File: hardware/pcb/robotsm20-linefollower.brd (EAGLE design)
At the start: 160 x 100 mm, 120 parts, among them IC1 BNO055, IC2 TPS43061RTER, Q1 CSD15571Q2, Q2 CSD15571Q2, Q3 CSD15571Q2, Q4 CSD15571Q2, Q5 BSS138LT3G, Q6 BSS138LT3G, Q7 BSS138LT3G, U1 STM32F405RG

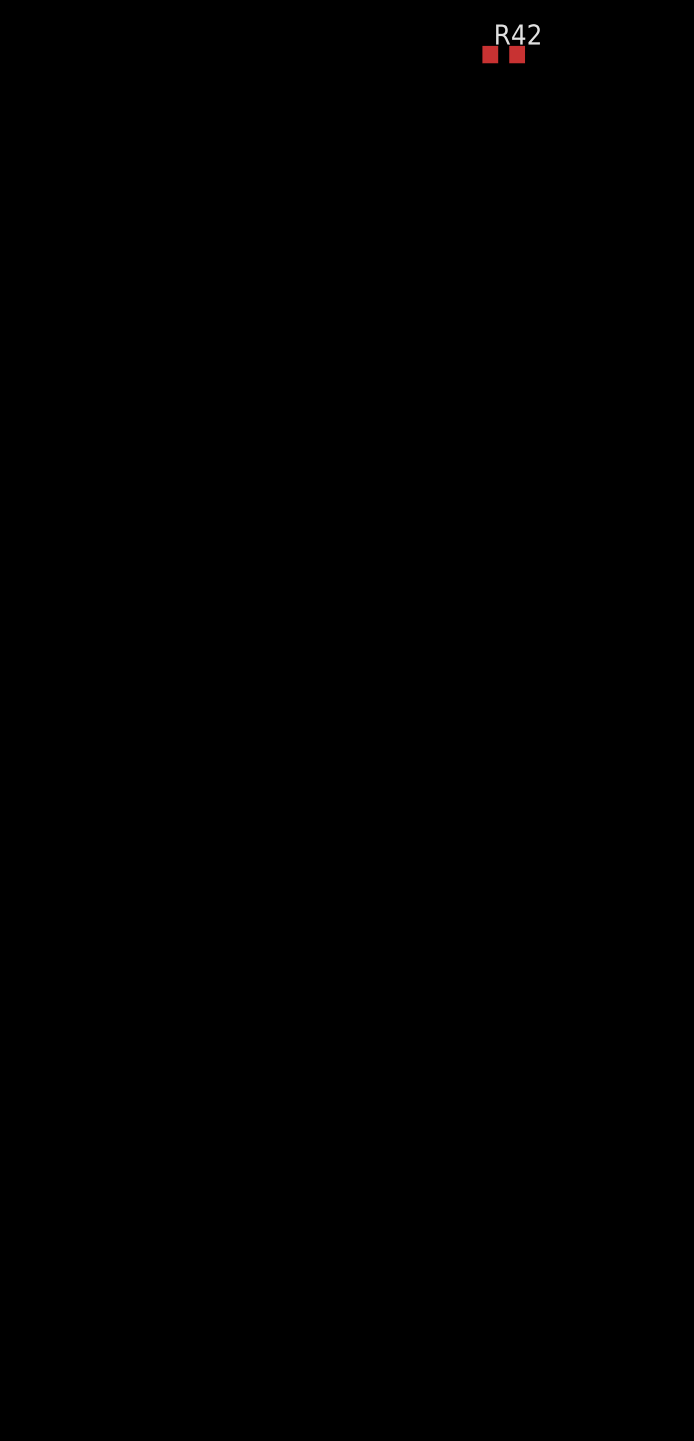
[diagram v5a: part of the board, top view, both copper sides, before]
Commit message: Added more connectors to motors and sensor
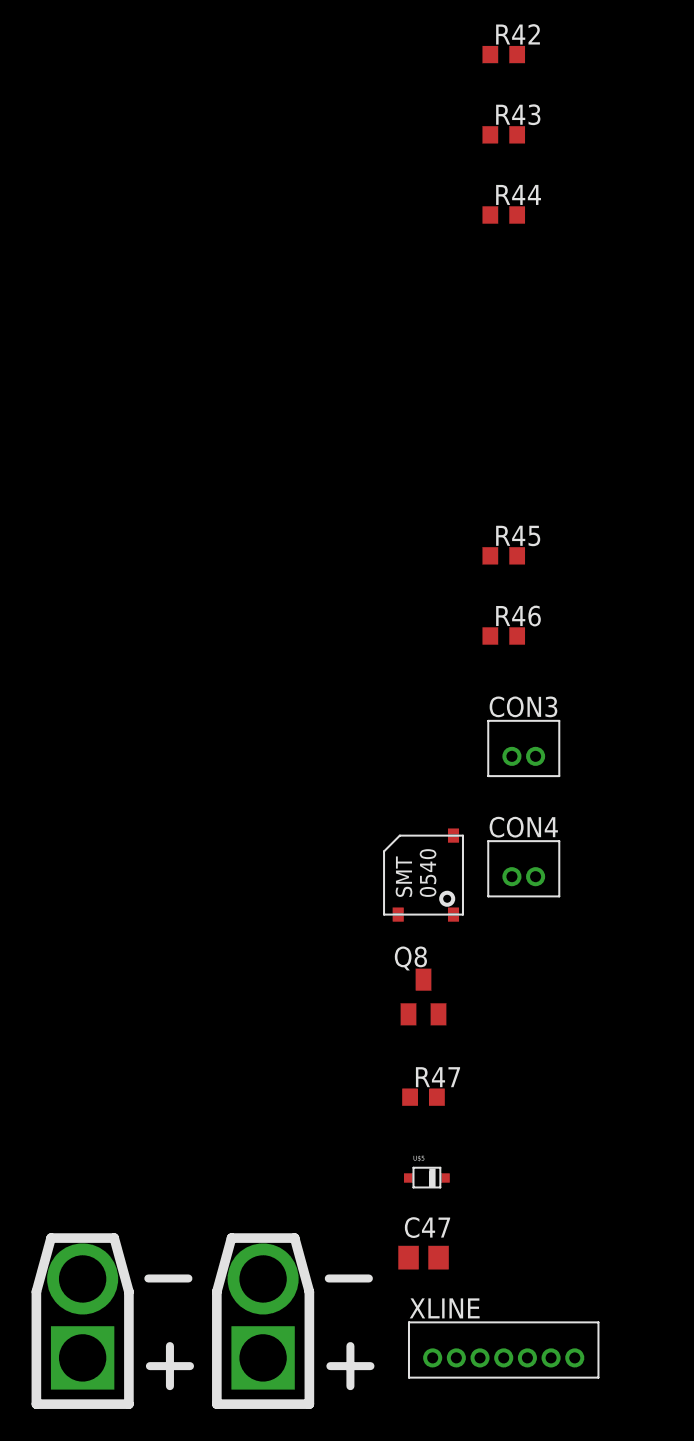
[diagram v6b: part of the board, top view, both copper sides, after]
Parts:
- added C47: (no value), rcl:C0805
- added CON3, CON4: ZR_B2B-ZR, CASE-JST:B2B-ZR
- added Q8: BSS138LT3G, CASE-Transistors:SOT23
- added R43: 20k, rcl:R0603
- added R44, R45, R47: 10k, rcl:R0603
- added R46: 62k, rcl:R0603
- added U$1: SMT-0540-S-R, Isaks Bibliotek:SMT-0540-S-R
- added U$5: DIODE_1N4148WX, Isaks Bibliotek:1N4148WX_SOD-323-2
- added U$8, U$9: XT30, CASE_DC-Connector:XT30
- added XLINE: ZH, CASE-JST:B7B-ZR
- R32: value 245R -> 300R
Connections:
- net N$66 renamed SDIO_CK
- net N$80 renamed SDIO_D0
- net VOLTM_CELL1 renamed N$25
- removed net 3.3V: BOOT.1, BOOT.2, C31.1, C32.1, C33.1, C34.1, C35.1, C37.1, C39.1, R30.1, R31.1, U1.1, U1.13, U1.19, U1.32, U1.48, U1.64
- removed net 3.3V1: R41.1, R42.1
- removed net CURA: C1.1, R3.2
- removed net CURB: C2.1, R4.2
- removed net GND1: PS2.3
- removed net INTERFACE_BUT1: C46.1, R35.1
- removed net N$10: PS2.9, R8.1
- removed net N$25 (its old number): U1.8
- removed net N$35: U1.11
- removed net N$82: U1.37
- removed net N$83: U1.38
- removed net V+1: C14.1, PS2.1, PS2.2
- new net MOTOR_L_CUR: C1.1, R3.2, U1.8
- new net MOTOR_R_CUR: C2.1, R4.2, U1.9
- new net PWM_FAN_L: CON3.1, U1.37
- new net PWM_FAN_R: CON4.1, U1.38
- new net SDIO_CMD: U1.54
- net +12V: now also R46.2
- net +3V3: now also BOOT.1, BOOT.2, C31.1, C32.1, C33.1, C34.1, C35.1, C37.1, C39.1, C47.1, R30.1, R31.1, R41.1, R42.1, U$1.+, U$5.-, U1.1, U1.13, U1.19, U1.32, U1.48, U1.64, XLINE.2
- net BTN_SEL: now also C46.1, R35.1, U1.11; no longer U1.54
- net BUZZER: now also Q8.1, R47.1
- net GND: now also CON3.2, CON4.2, PS2.3, PS2.9, Q8.2, R44.2, R45.1, R47.2, R8.1, U$8.NEG-, U$9.NEG-, XLINE.1
- net MUX0: now also XLINE.4
- net MUX1: now also XLINE.5
- net MUX2: now also XLINE.6
- net MUX3: now also XLINE.7
- net N$33: now also C47.2, Q8.3, U$1.-, U$5.+; no longer U1.9
- net V+: now also C14.1, PS2.1, PS2.2, R43.1, U$8.POS+, U$9.POS+
- net VOLTM_BATT: now also R43.2, R44.1, R45.2, R46.1
- net XLINE: now also XLINE.3

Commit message: Corrected some ERC
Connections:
- removed net N$2: MOTORDRIVER.26, MOTORDRIVER.27
- removed net N$36: C43.1
- net +3V3: now also C43.1
- net 12V: now also MOTORDRIVER.26, MOTORDRIVER.27
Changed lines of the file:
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@@
 <contactref element="XLINE" pad="1"/>
 <contactref element="U$8" pad="NEG-"/>
-<contactref element="U$9" pad="NEG-"/>
 <contactref element="R8" pad="1"/>
 <contactref element="PS2" pad="9"/>
 <contactref element="PS2" pad="3"/>
+<contactref element="U$9" pad="NEG-"/>
 <wire x1="-53.66" y1="-186.69" x2="-53.66" y2="-193.04" width="0" layer="19" extent="1-1"/>
 <wire x1="-53.66" y1="-180.34" x2="-53.66" y2="-186.69" width="0" layer="19" extent="1-1"/>
@@
 <wire x1="124.25" y1="45.3856" x2="123.61" y2="53.34" width="0" layer="19" extent="1-1"/>
 </signal>
-<signal name="N$2">
-<contactref element="MOTORDRIVER" pad="26"/>
-<contactref element="MOTORDRIVER" pad="27"/>
-<wire x1="130.4756" y1="40.16" x2="130.4756" y2="39.66" width="0" layer="19" extent="1-1"/>
-</signal>
 <signal name="12V">
 <contactref element="MOTORDRIVER" pad="10"/>
@@
 <contactref element="C5" pad="1"/>
 <contactref element="C4" pad="1"/>
+<contactref element="MOTORDRIVER" pad="26"/>
+<contactref element="MOTORDRIVER" pad="27"/>
 <wire x1="132.08" y1="37.78" x2="137.16" y2="39.63" width="0" layer="19" extent="1-1"/>
-<wire x1="123.5244" y1="39.66" x2="132.08" y2="37.78" width="0" layer="19" extent="1-1"/>
-<wire x1="123.5244" y1="40.16" x2="123.5244" y2="39.66" width="0" layer="19" extent="1-1"/>
+<wire x1="130.4756" y1="39.66" x2="132.08" y2="37.78" width="0" layer="19" extent="1-1"/>
+<wire x1="130.4756" y1="40.16" x2="130.4756" y2="39.66" width="0" layer="19" extent="1-1"/>
+<wire x1="123.5244" y1="40.16" x2="130.4756" y2="40.16" width="0" layer="19" extent="1-1"/>
+<wire x1="123.5244" y1="39.66" x2="123.5244" y2="40.16" width="0" layer="19" extent="1-1"/>
 <wire x1="121.92" y1="37.78" x2="123.5244" y2="39.66" width="0" layer="19" extent="1-1"/>
 <wire x1="116.84" y1="39.63" x2="121.92" y2="37.78" width="0" layer="19" extent="1-1"/>
@@
 <contactref element="R30" pad="1"/>
 <contactref element="R31" pad="1"/>
+<contactref element="C43" pad="1"/>
 <wire x1="-55.56" y1="-180.34" x2="-55.56" y2="-193.04" width="0" layer="19" extent="1-1"/>
 <wire x1="-55.56" y1="-167.64" x2="-55.56" y2="-180.34" width="0" layer="19" extent="1-1"/>
@@
 <wire x1="-67.83" y1="-80.01" x2="-53.28" y2="-126.4087" width="0" layer="19" extent="1-1"/>
 <wire x1="-67.83" y1="-74.93" x2="-67.83" y2="-80.01" width="0" layer="19" extent="1-1"/>
-<wire x1="-32.17" y1="-27.94" x2="-67.83" y2="-74.93" width="0" layer="19" extent="1-1"/>
+<wire x1="-33.97" y1="-30.48" x2="-67.83" y2="-74.93" width="0" layer="19" extent="1-1"/>
+<wire x1="-32.17" y1="-27.94" x2="-33.97" y2="-30.48" width="0" layer="19" extent="1-1"/>
 <wire x1="-28.92" y1="-26.42" x2="-32.17" y2="-27.94" width="0" layer="19" extent="1-1"/>
 <wire x1="-28.42" y1="-25.12" x2="-28.92" y2="-26.42" width="0" layer="19" extent="1-1"/>
@@
 <wire x1="120.43" y1="4.755" x2="123.61" y2="10.16" width="0" layer="19" extent="1-1"/>
 </signal>
-<signal name="N$1">
-</signal>
 <signal name="N$6">
 <contactref element="R7" pad="1"/>
@@
 <wire x1="-28.92" y1="-26.92" x2="-33.87" y2="-27.94" width="0" layer="19" extent="1-1"/>
 </signal>
-<signal name="N$36">
-<contactref element="C43" pad="1"/>
-</signal>
 <signal name="N$27">

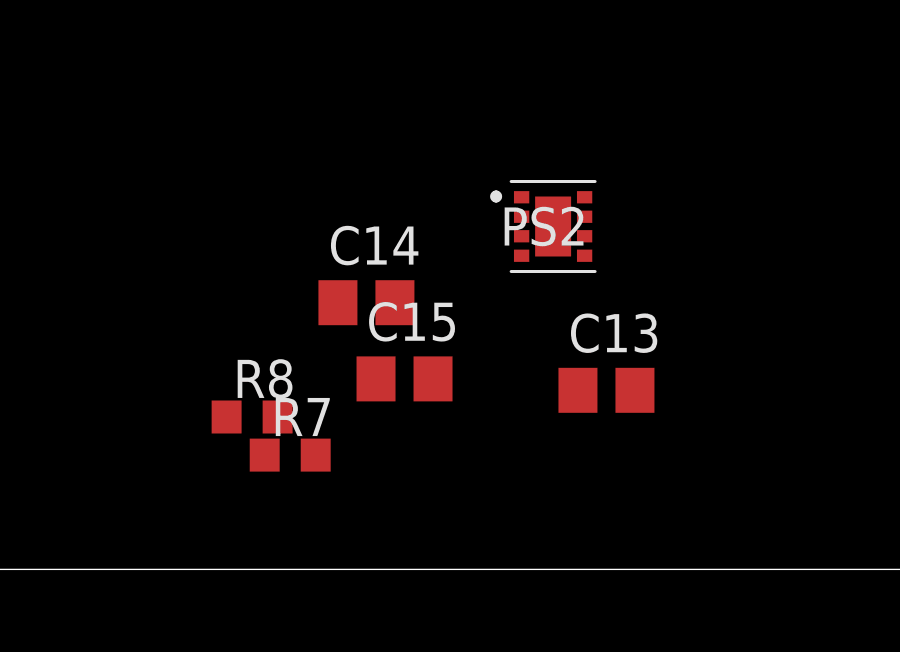
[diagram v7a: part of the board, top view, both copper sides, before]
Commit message: Deleted 3V7 buck
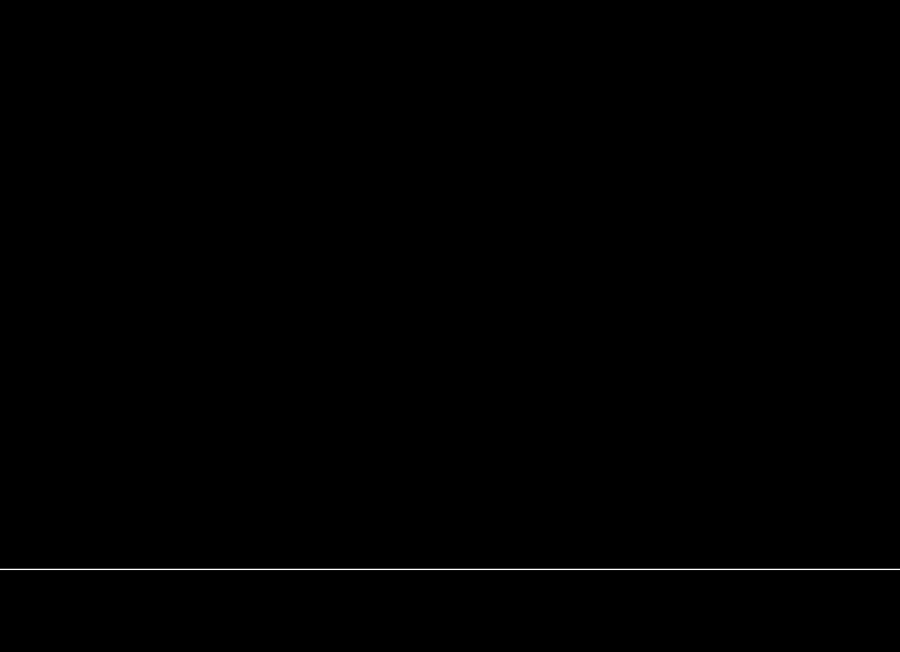
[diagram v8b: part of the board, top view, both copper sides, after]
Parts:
- removed C13, C14: 22µF, rcl:C0805
- removed C15: 3300pF, rcl:C0805
- removed PS2: TPS82130SILT, PowerManagement:TPS82130SILT
- removed R7: 36.25k, rcl:R0603
- removed R8: 10k, rcl:R0603
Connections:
- removed net 3V7: C13.1, PS2.4, PS2.5, R7.2
- removed net N$5: C15.1, PS2.8
- removed net N$6: PS2.6, R7.1, R8.2
- net GND: no longer C13.2, C14.2, C15.2, PS2.3, PS2.9, R8.1
- net V+: no longer C14.1, PS2.1, PS2.2
